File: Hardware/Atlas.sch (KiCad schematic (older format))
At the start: 10 parts

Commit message: Change to bottom shield, remove arduino pins
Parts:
- removed H?: NUCLEO-F401, ~, symbol NUCLEO-F401
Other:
- moved on the sheet: H?B, H?C, U?
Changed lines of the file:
@@
 Sheet 1 1
 Title ""
-Date "21 may 2014"
+Date "22 may 2014"
 Rev ""
 Comp ""
@@
 $Comp
 L NUCLEO-F401 H?
-U 1 1 537D23D5
-P 2300 1900
-F 0 "H?" H 2300 2900 60  0000 C CNN
-F 1 "NUCLEO-F401" V 2300 1900 60  0000 C CNN
-F 2 "~" H 2300 1900 60  0000 C CNN
-F 3 "~" H 2300 1900 60  0000 C CNN
-	1    2300 1900
-	1    0    0    -1
-$EndComp
-$Comp
-L NUCLEO-F401 H?
 U 2 1 537D23EE
-P 2300 4100
-F 0 "H?" H 2300 5100 60  0000 C CNN
-F 1 "NUCLEO-F401" V 2300 4100 60  0000 C CNN
-F 2 "~" H 2300 4100 60  0000 C CNN
-F 3 "~" H 2300 4100 60  0000 C CNN
-	2    2300 4100
+P 2300 4200
+F 0 "H?" H 2300 5200 60  0000 C CNN
+F 1 "NUCLEO-F401" V 2300 4200 60  0000 C CNN
+F 2 "~" H 2300 4200 60  0000 C CNN
+F 3 "~" H 2300 4200 60  0000 C CNN
+	2    2300 4200
 	1    0    0    -1
 $EndComp
@@
 L NUCLEO-F401 H?
 U 3 1 537D23FD
-P 2300 6300
-F 0 "H?" H 2300 7300 60  0000 C CNN
-F 1 "NUCLEO-F401" V 2300 6300 60  0000 C CNN
-F 2 "~" H 2300 6300 60  0000 C CNN
-F 3 "~" H 2300 6300 60  0000 C CNN
-	3    2300 6300
+P 9700 4200
+F 0 "H?" H 9700 5200 60  0000 C CNN
+F 1 "NUCLEO-F401" V 9700 4200 60  0000 C CNN
+F 2 "~" H 9700 4200 60  0000 C CNN
+F 3 "~" H 9700 4200 60  0000 C CNN
+	3    9700 4200
 	1    0    0    -1
 $EndComp
-Text Label 3200 1400 0    60   ~ 0
+Text Label 8800 3800 2    60   ~ 0
 SCK
-Text Label 3200 1500 0    60   ~ 0
+Text Label 8800 3900 2    60   ~ 0
 MISO
-Text Label 3200 1600 0    60   ~ 0
+Text Label 8800 4000 2    60   ~ 0
 MOSI
-Text Label 3200 1700 0    60   ~ 0
+Text Label 8800 4100 2    60   ~ 0
 CS
-Text Label 3200 1000 0    60   ~ 0
+Text Label 8800 3400 2    60   ~ 0
 SCL
 Wire Wire Line
-	2800 1000 3200 1000
-Text Label 3200 1100 0    60   ~ 0
+	9200 3400 8800 3400
+Text Label 8800 3500 2    60   ~ 0
 SDA
 Wire Wire Line
-	3200 1100 2800 1100
-Text Notes 2900 2800 0    60   Italic 0
+	8800 3500 9200 3500
+Text Notes 9100 5100 2    60   Italic 0
 D0
-Text Notes 2900 2700 0    60   Italic 0
+Text Notes 9100 5000 2    60   Italic 0
 D1
-Text Notes 2900 2600 0    60   Italic 0
+Text Notes 9100 4900 2    60   Italic 0
 D2
-Text Notes 2900 2500 0    60   Italic 0
+Text Notes 9100 4800 2    60   Italic 0
 D3
-Text Notes 2900 2400 0    60   Italic 0
+Text Notes 9100 4700 2    60   Italic 0
 D4
-Text Notes 2900 2300 0    60   Italic 0
+Text Notes 9100 4600 2    60   Italic 0
 D5
-Text Notes 2900 2200 0    60   Italic 0
+Text Notes 9100 4500 2    60   Italic 0
 D6
-Text Notes 2900 2100 0    60   Italic 0
+Text Notes 9100 4400 2    60   Italic 0
 D7
-Text Notes 2900 1900 0    60   Italic 0
+Text Notes 9100 4300 2    60   Italic 0
 D8
-Text Notes 2900 1800 0    60   Italic 0
+Text Notes 9100 4200 2    60   Italic 0
 D9
-Text Notes 2900 1700 0    60   Italic 0
+Text Notes 9100 4100 2    60   Italic 0
 D10
-Text Notes 2900 1600 0    60   Italic 0
+Text Notes 9100 4000 2    60   Italic 0
 D11
-Text Notes 2900 1500 0    60   Italic 0
+Text Notes 9100 3900 2    60   Italic 0
 D12
-Text Notes 2900 1400 0    60   Italic 0
+Text Notes 9100 3800 2    60   Italic 0
 D13
 Wire Wire Line
-	2800 1400 3200 1400
+	9200 3800 8800 3800
 Wire Wire Line
-	2800 1500 3200 1500
+	9200 3900 8800 3900
 Wire Wire Line
-	2800 1600 3200 1600
+	9200 4000 8800 4000
 Wire Wire Line
-	2800 1700 3200 1700
-Text Notes 2900 1100 0    60   Italic 0
+	9200 4100 8800 4100
+Text Notes 9100 3500 2    60   Italic 0
 D14
-Text Notes 2900 1000 0    60   Italic 0
+Text Notes 9100 3400 2    60   Italic 0
 D15
-Text Notes 1700 2300 2    60   Italic 0
+Text Notes 2900 4600 0    60   Italic 0
 A0
-Text Notes 1700 2400 2    60   Italic 0
+Text Notes 2900 4700 0    60   Italic 0
 A1
-Text Notes 1700 2500 2    60   Italic 0
+Text Notes 2900 4800 0    60   Italic 0
 A2
-Text Notes 1700 2600 2    60   Italic 0
+Text Notes 2900 4900 0    60   Italic 0
 A3
-Text Notes 1700 2700 2    60   Italic 0
+Text Notes 2900 5000 0    60   Italic 0
 A4
-Text Notes 1700 2800 2    60   Italic 0
+Text Notes 2900 5100 0    60   Italic 0
 A5
 $Comp
 L MPU9150 U?
 U 1 1 537D23AC
-P 8800 1800
-F 0 "U?" H 8800 2300 60  0000 C CNN
-F 1 "MPU9150" V 8800 1800 60  0000 C CNN
-F 2 "~" H 8800 1800 60  0000 C CNN
-F 3 "~" H 8800 1800 60  0000 C CNN
-	1    8800 1800
+P 6750 1850
+F 0 "U?" H 6750 2350 60  0000 C CNN
+F 1 "MPU9150" V 6750 1850 60  0000 C CNN
+F 2 "~" H 6750 1850 60  0000 C CNN
+F 3 "~" H 6750 1850 60  0000 C CNN
+	1    6750 1850
 	1    0    0    -1
 $EndComp
@@
 L MS5611 U?
 U 1 1 537D23BB
-P 8700 2850
-F 0 "U?" H 8700 3100 60  0000 C CNN
-F 1 "MS5611" V 8700 2850 60  0000 C CNN
-F 2 "~" H 8700 2850 60  0000 C CNN
-F 3 "~" H 8700 2850 60  0000 C CNN
-	1    8700 2850
+P 6650 2900
+F 0 "U?" H 6650 3150 60  0000 C CNN
+F 1 "MS5611" V 6650 2900 60  0000 C CNN
+F 2 "~" H 6650 2900 60  0000 C CNN
+F 3 "~" H 6650 2900 60  0000 C CNN
+	1    6650 2900
 	1    0    0    -1
 $EndComp
@@
 L SHT21 U?
 U 1 1 537D23CA
-P 8700 3850
-F 0 "U?" H 8700 4150 60  0000 C CNN
-F 1 "HTU21D" H 8700 3550 60  0000 C CNN
-F 2 "~" H 8700 3850 60  0000 C CNN
-F 3 "~" H 8700 3850 60  0000 C CNN
-	1    8700 3850
+P 6650 3900
+F 0 "U?" H 6650 4200 60  0000 C CNN
+F 1 "HTU21D" H 6650 3600 60  0000 C CNN
+F 2 "~" H 6650 3900 60  0000 C CNN
+F 3 "~" H 6650 3900 60  0000 C CNN
+	1    6650 3900
 	1    0    0    -1
 $EndComp
@@
 L SDCARD-FULL-MICRO U?
 U 1 1 537D2B6A
-P 9700 6150
-F 0 "U?" H 9700 6600 60  0000 C CNN
-F 1 "SDCARD-FULL-MICRO" H 9700 5700 60  0000 C CNN
-F 2 "~" H 9700 6150 60  0000 C CNN
-F 3 "~" H 9700 6150 60  0000 C CNN
-	1    9700 6150
+P 7650 6200
+F 0 "U?" H 7650 6650 60  0000 C CNN
+F 1 "SDCARD-FULL-MICRO" H 7650 5750 60  0000 C CNN
+F 2 "~" H 7650 6200 60  0000 C CNN
+F 3 "~" H 7650 6200 60  0000 C CNN
+	1    7650 6200
 	-1   0    0    -1
 $EndComp
@@
 L RFD900 U?
 U 1 1 537D3811
-P 6100 5750
-F 0 "U?" H 6100 6200 60  0000 C CNN
-F 1 "RFD900" H 6100 5300 60  0000 C CNN
-F 2 "" H 6100 5000 60  0000 C CNN
-F 3 "" H 6100 5000 60  0000 C CNN
-	1    6100 5750
+P 4050 5800
+F 0 "U?" H 4050 6250 60  0000 C CNN
+F 1 "RFD900" H 4050 5350 60  0000 C CNN
+F 2 "" H 4050 5050 60  0000 C CNN
+F 3 "" H 4050 5050 60  0000 C CNN
+	1    4050 5800
 	1    0    0    -1
 $EndComp
@@
 L XTEND U?
 U 1 1 537D3820
-P 7500 5900
-F 0 "U?" H 7500 6500 60  0000 C CNN
-F 1 "XTEND" H 7500 5300 60  0000 C CNN
-F 2 "~" H 7500 5900 60  0000 C CNN
-F 3 "~" H 7500 5900 60  0000 C CNN
-	1    7500 5900
+P 5450 5950
+F 0 "U?" H 5450 6550 60  0000 C CNN
+F 1 "XTEND" H 5450 5350 60  0000 C CNN
+F 2 "~" H 5450 5950 60  0000 C CNN
+F 3 "~" H 5450 5950 60  0000 C CNN
+	1    5450 5950
 	1    0    0    -1
 $EndComp
@@
 L XBEE U?
 U 1 1 537D382F
-P 6150 4250
-F 0 "U?" H 6150 4800 60  0000 C CNN
-F 1 "XBEE" H 6150 3700 60  0000 C CNN
-F 2 "~" H 6700 3300 60  0000 C CNN
-F 3 "~" H 6700 3300 60  0000 C CNN
-	1    6150 4250
+P 4100 4300
+F 0 "U?" H 4100 4850 60  0000 C CNN
+F 1 "XBEE" H 4100 3750 60  0000 C CNN
+F 2 "~" H 4650 3350 60  0000 C CNN
+F 3 "~" H 4650 3350 60  0000 C CNN
+	1    4100 4300
 	1    0    0    -1
 $EndComp

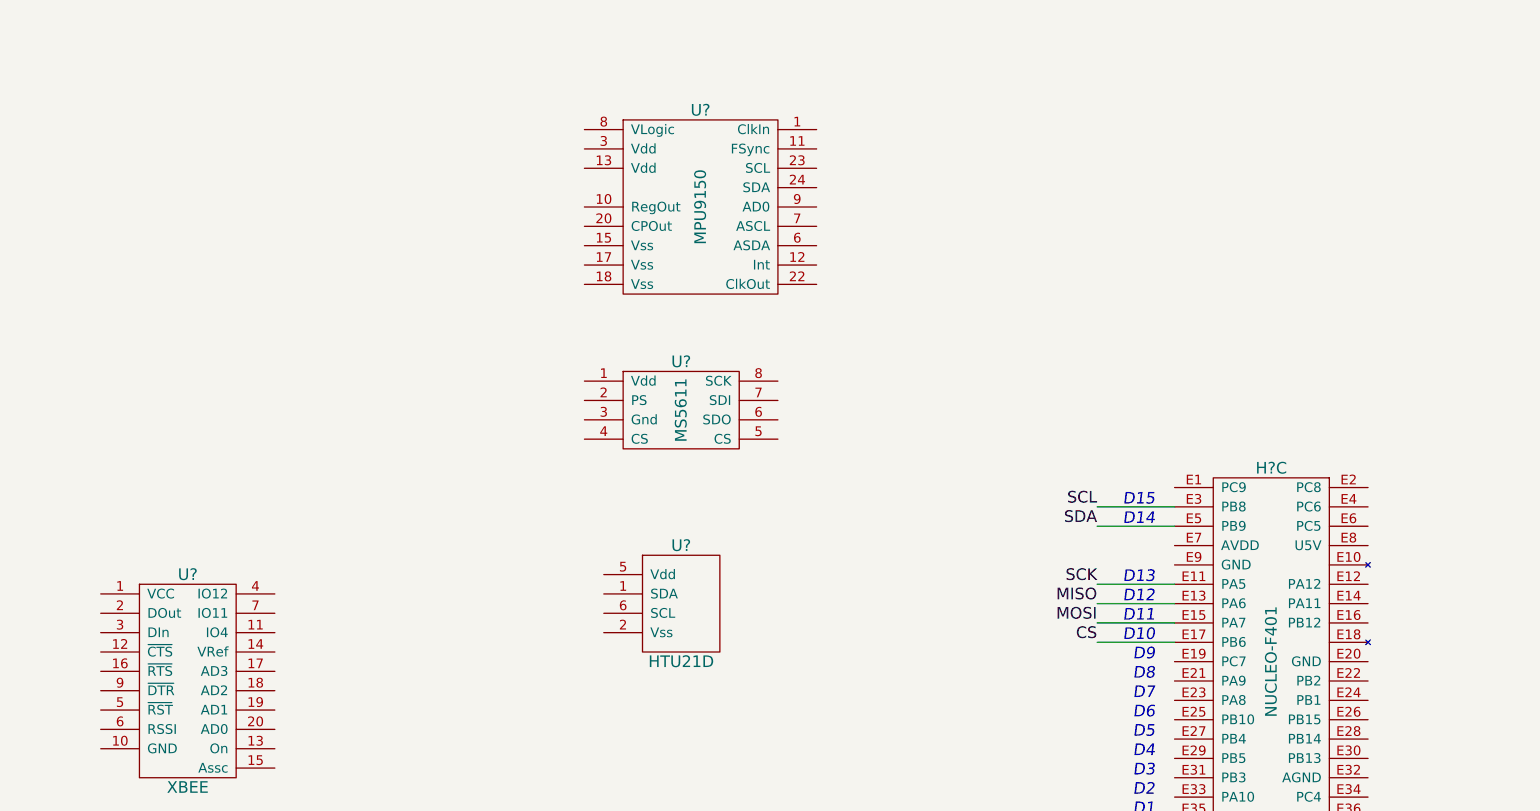
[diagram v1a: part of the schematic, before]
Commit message: Add sensor support components
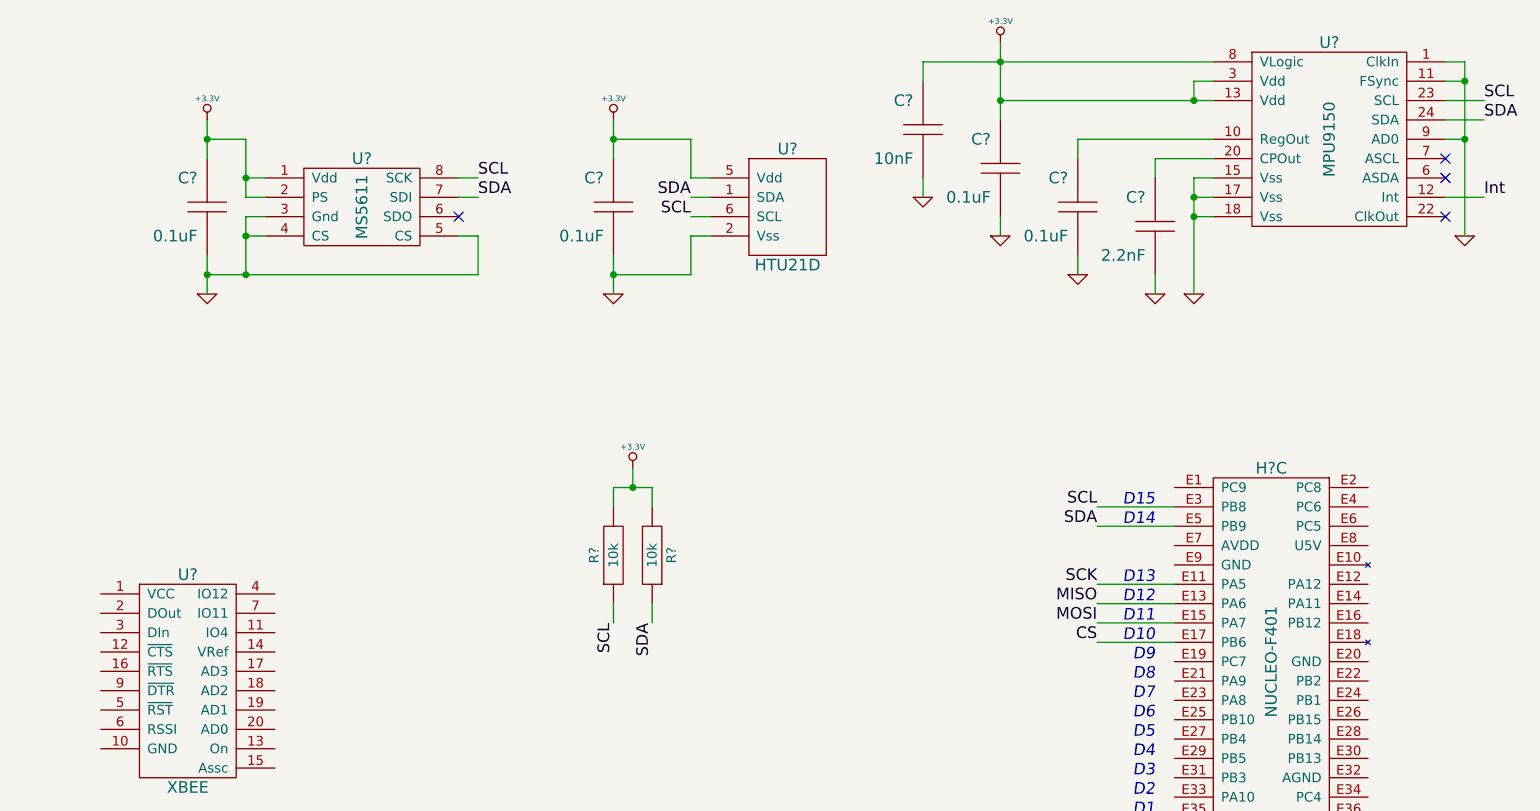
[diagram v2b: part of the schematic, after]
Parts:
- added C? (x4): 0.1uF, CAPC1608-N, symbol C
- added C?: 2.2nF, ~, symbol C
- added C?: 10nF, ~, symbol C
- added R? (x2): 10k, RESC1608-N, symbol R
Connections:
- net labels added: +3.3V, GND, Int
- wire segments 6 -> 61
- no-connect marks 0 -> 4
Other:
- moved on the sheet: U?

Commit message: Wire SD Card
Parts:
- added C?: 0.1uF, CAPC1608-N, symbol C
- U?: value SDCARD-FULL-MICRO -> uSD Card
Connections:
- wire segments 61 -> 69
- no-connect marks 4 -> 6
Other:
- moved on the sheet: U?
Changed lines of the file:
@@
 L SDCARD-FULL-MICRO U?
 U 1 1 537D2B6A
-P 7650 6200
-F 0 "U?" H 7650 6650 60  0000 C CNN
-F 1 "SDCARD-FULL-MICRO" H 7650 5750 60  0000 C CNN
-F 2 "~" H 7650 6200 60  0000 C CNN
-F 3 "~" H 7650 6200 60  0000 C CNN
-	1    7650 6200
+P 7700 5550
+F 0 "U?" H 7700 6000 60  0000 C CNN
+F 1 "uSD Card" H 7700 5100 60  0000 C CNN
+F 2 "~" H 7700 5550 60  0000 C CNN
+F 3 "~" H 7700 5550 60  0000 C CNN
+	1    7700 5550
 	-1   0    0    -1
 $EndComp
@@
 $EndComp
 Wire Wire Line
-	9300 2300 9300 1700
+	9300 1700 9300 2300
 Wire Wire Line
 	9300 1700 9400 1700
@@
 $EndComp
 Wire Wire Line
-	10700 2000 10700 1100
+	10700 1100 10700 2000
 Wire Wire Line
 	10700 1100 10600 1100
@@
 Wire Wire Line
 	10800 1800 10600 1800
+$Comp
+L C C?
+U 1 1 537E5FB0
+P 6800 5550
+F 0 "C?" H 6850 5700 60  0000 L CNN
+F 1 "0.1uF" H 6850 5400 60  0000 L CNN
+F 2 "CAPC1608-N" H 6800 5550 60  0001 C CNN
+F 3 "~" H 6800 5550 60  0000 C CNN
+F 4 "Samsung" H 6800 5550 60  0001 C CNN "MFR Name"
+F 5 "CL10B104KO8NNNC" H 6800 5550 60  0001 C CNN "MFR Part No"
+F 6 "1276-1005-1-ND" H 6800 5550 60  0001 C CNN "Distributor Part No"
+F 7 "16V" H 6750 5400 60  0001 R CNN "Voltage"
+F 8 "X7R" H 6750 5700 60  0001 R CNN "Dielectric"
+	1    6800 5550
+	-1   0    0    -1
+$EndComp
+Text Label 7200 5300 2    60   ~ 0
+MOSI
+Text Label 7200 5400 2    60   ~ 0
+SCK
+Text Label 7200 5500 2    60   ~ 0
+MISO
+Text Label 7200 5800 2    60   ~ 0
+CS
+NoConn ~ 7300 5700
+$Comp
+L +3.3V #PWR?
+U 1 1 537E6063
+P 6800 5100
+F 0 "#PWR?" H 6800 5060 30  0001 C CNN
+F 1 "+3.3V" H 6800 5210 30  0000 C CNN
+F 2 "" H 6800 5100 60  0000 C CNN
+F 3 "" H 6800 5100 60  0000 C CNN
+	1    6800 5100
+	1    0    0    -1
+$EndComp
+Wire Wire Line
+	6800 5100 6800 5300
+Wire Wire Line
+	7300 5200 6800 5200
+Connection ~ 6800 5200
+$Comp
+L GND #PWR?
+U 1 1 537E612B
+P 6800 6000
+F 0 "#PWR?" H 6800 6000 30  0001 C CNN
+F 1 "GND" H 6800 5930 30  0001 C CNN
+F 2 "" H 6800 6000 60  0000 C CNN
+F 3 "" H 6800 6000 60  0000 C CNN
+	1    6800 6000
+	1    0    0    -1
+$EndComp
+Wire Wire Line
+	6800 5800 6800 6000
+Wire Wire Line
+	7300 5900 6800 5900
+Connection ~ 6800 5900
+Wire Wire Line
+	7200 5300 7300 5300
+Wire Wire Line
+	7200 5400 7300 5400
+Wire Wire Line
+	7200 5500 7300 5500
+Wire Wire Line
+	7200 5800 7300 5800
+NoConn ~ 7300 5600
 $EndSCHEMATC

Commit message: Layout schematic to reflect board
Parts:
- C?: value 2.2nF -> 2200pF; footprint ~ -> CAPC1608-N; Dielectric D -> X7R; Distributor Part No (none) -> 1276-1992-1-ND; MFR Name (none) -> Samsung; MFR Part No (none) -> CL10B222KB8SFNC; Voltage V -> 50V
- C?: value 10nF -> 10000pF; footprint ~ -> CAPC1608-N; Dielectric D -> X7R; Distributor Part No (none) -> 1276-1009-1-ND; MFR Name (none) -> Samsung; MFR Part No (none) -> CL10B103KB8NNNC; Voltage V -> 50V
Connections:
- wire segments 69 -> 87
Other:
- moved on the sheet: C?, R?, U?

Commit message: Remove XTend because it is stupid
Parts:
- removed U?: XTEND, ~, symbol XTEND
- added B?: 4AA, ~, symbol BATTERY
- U?: Distributor Part No (none) -> S5561-ND; MFR Name (none) -> Sullins; MFR Part No (none) -> PPPC082LJBN-RC
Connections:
- net labels added: +BATT
- wire segments 87 -> 71
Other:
- moved on the sheet: C?, H?B, H?C, R?, U?

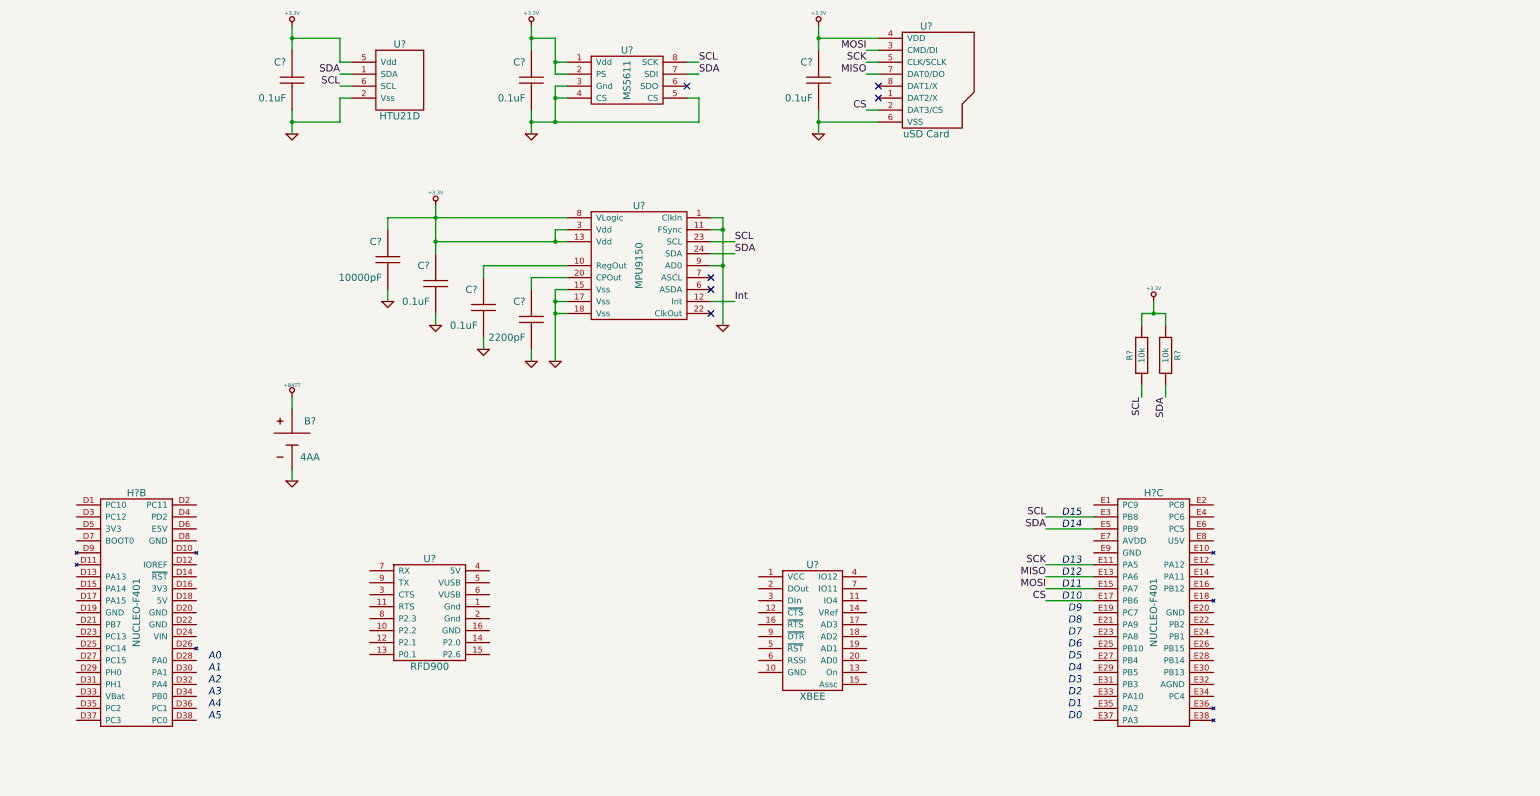
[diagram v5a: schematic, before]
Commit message: Add GPS to schematic
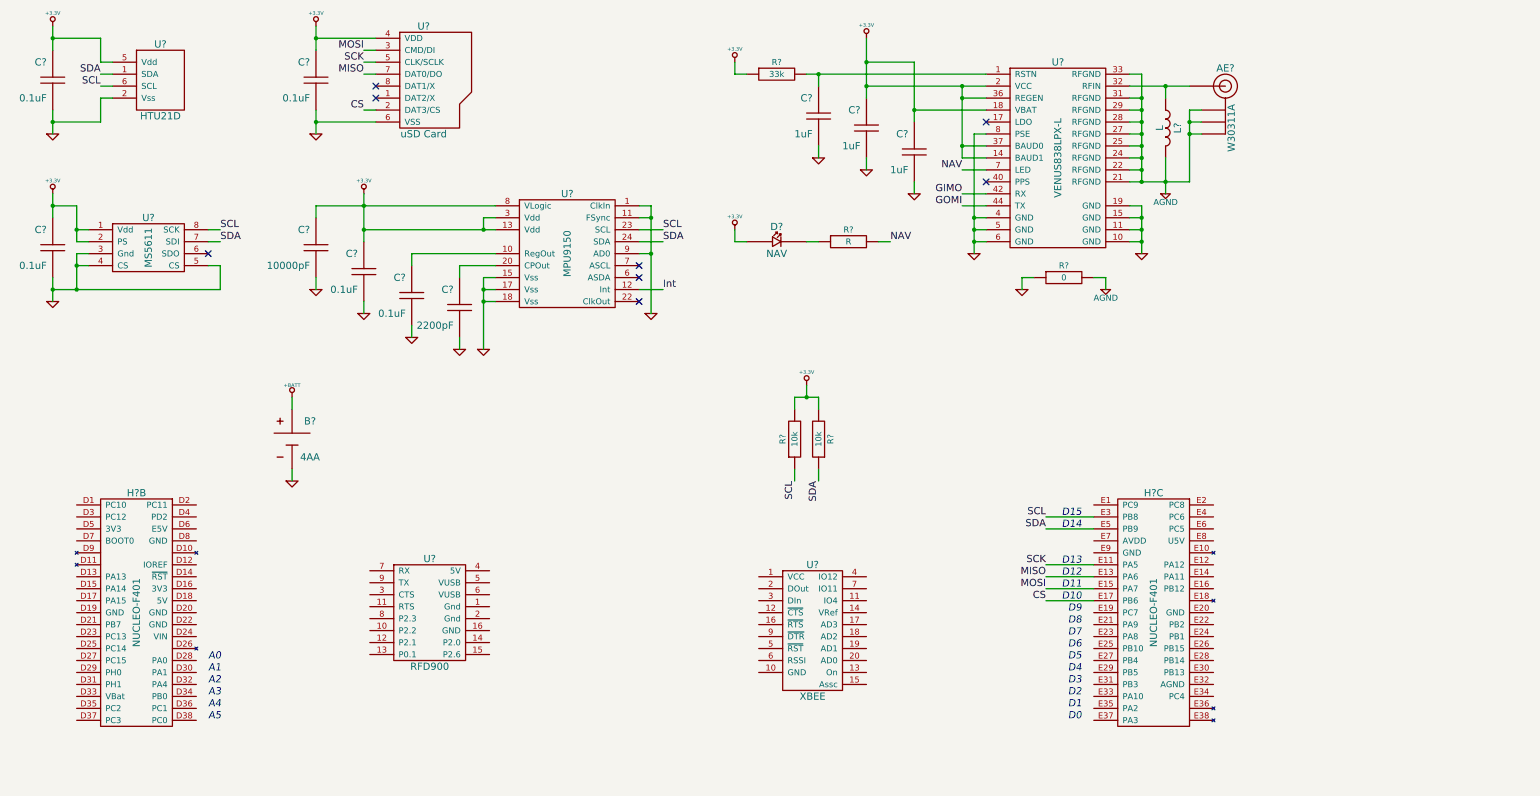
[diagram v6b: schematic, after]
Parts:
- added AE?: W30311A, ~, symbol ANTENNA
- added C? (x3): 1uF, CAPC1608-N, symbol C
- added D?: NAV, ~, symbol LED
- added L?: L, INDC1005-N, symbol L
- added R?: 33k, ~, symbol R
- added R?: R, ~, symbol R
- added R?: 0, RESC1608-N, symbol R
- added U?: VENUS838LPX-L, symbol VENUS838LPX-L
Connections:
- net +3.3V: now also C?.1, C?.1, D?.1, R?.1, U?.14 (BAUD1), U?.18 (VBAT), U?.2 (VCC), U?.36 (REGEN), U?.37 (BAUD0)
- net GND: now also C?.2, C?.2, C?.2, R?.1, U?.10 (GND), U?.11 (GND), U?.15 (GND), U?.19 (GND), U?.4 (GND), U?.5 (GND), U?.6 (GND), U?.8 (PSE)
- new net: C?.1, R?.2, U?.1 (RSTN)
- new net: AE?.P, L?.2, U?.32 (RFIN)
- new net: D?.2, R?.1
- new net AGND: AE?.S, L?.1, R?.2, U?.21 (RFGND), U?.22 (RFGND), U?.24 (RFGND), U?.25 (RFGND), U?.27 (RFGND), U?.28 (RFGND), U?.29 (RFGND), U?.31 (RFGND), U?.33 (RFGND)
- new net GIMO: U?.42 (RX)
- new net GOMI: U?.44 (TX)
- new net NAV: R?.2, U?.7 (LED)
- no-connect marks 6 -> 8
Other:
- moved on the sheet: C?, R?, U?
